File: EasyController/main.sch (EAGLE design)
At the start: 53 parts, among them IC2 L6387EDIP8, IC3 L6387EDIP8, IC4 L6387EDIP8, J3 FUSE, Q1 MOSFET-NCHANNELTO-220-FLAT, Q2 MOSFET-NCHANNELTO-220-FLAT, Q3 MOSFET-NCHANNELTO-220-FLAT, Q4 MOSFET-NCHANNELTO-220-FLAT, Q5 MOSFET-NCHANNELTO-220-FLAT, Q6 MOSFET-NCHANNELTO-220-FLAT

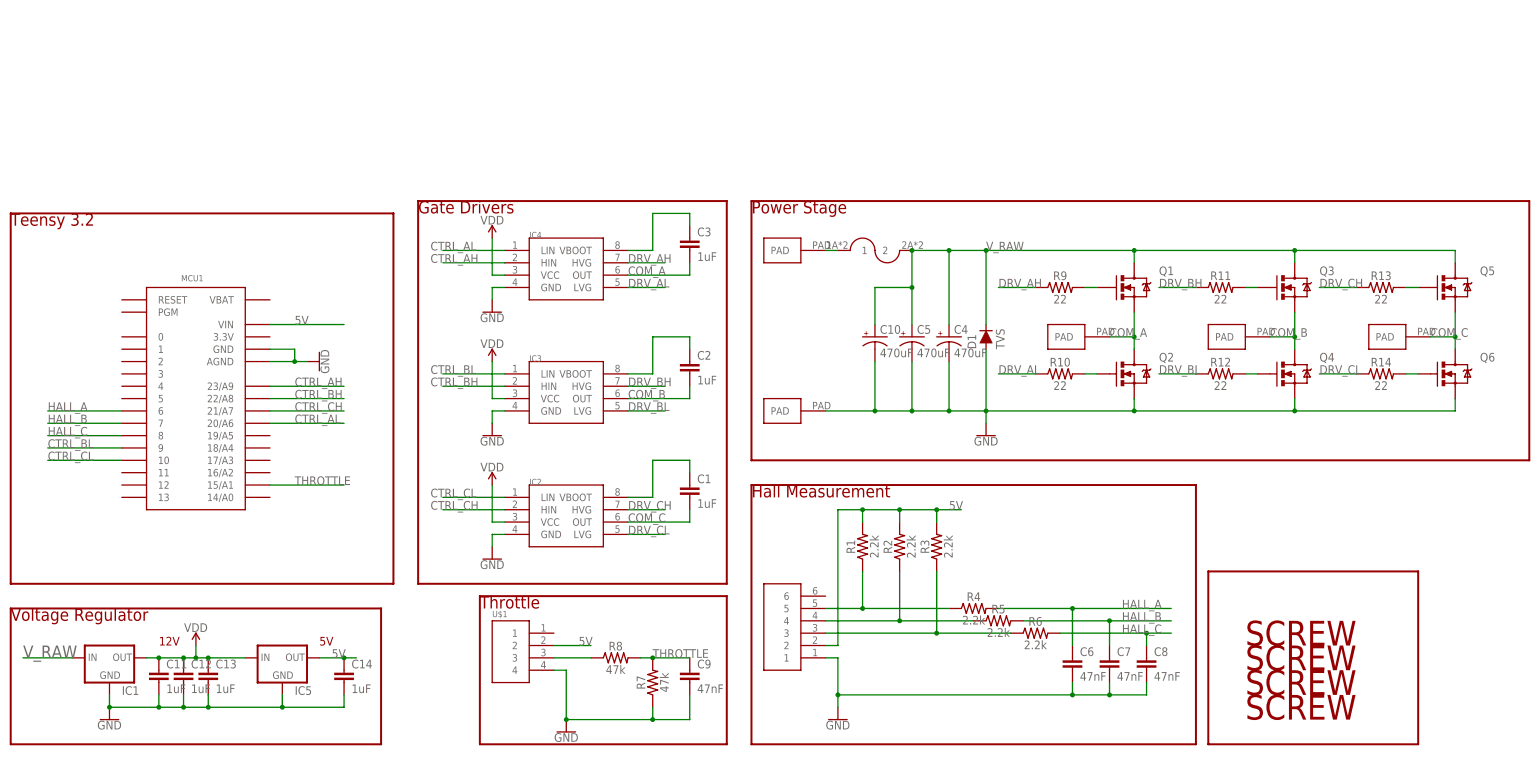
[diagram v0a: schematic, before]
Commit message: CAN transceiver
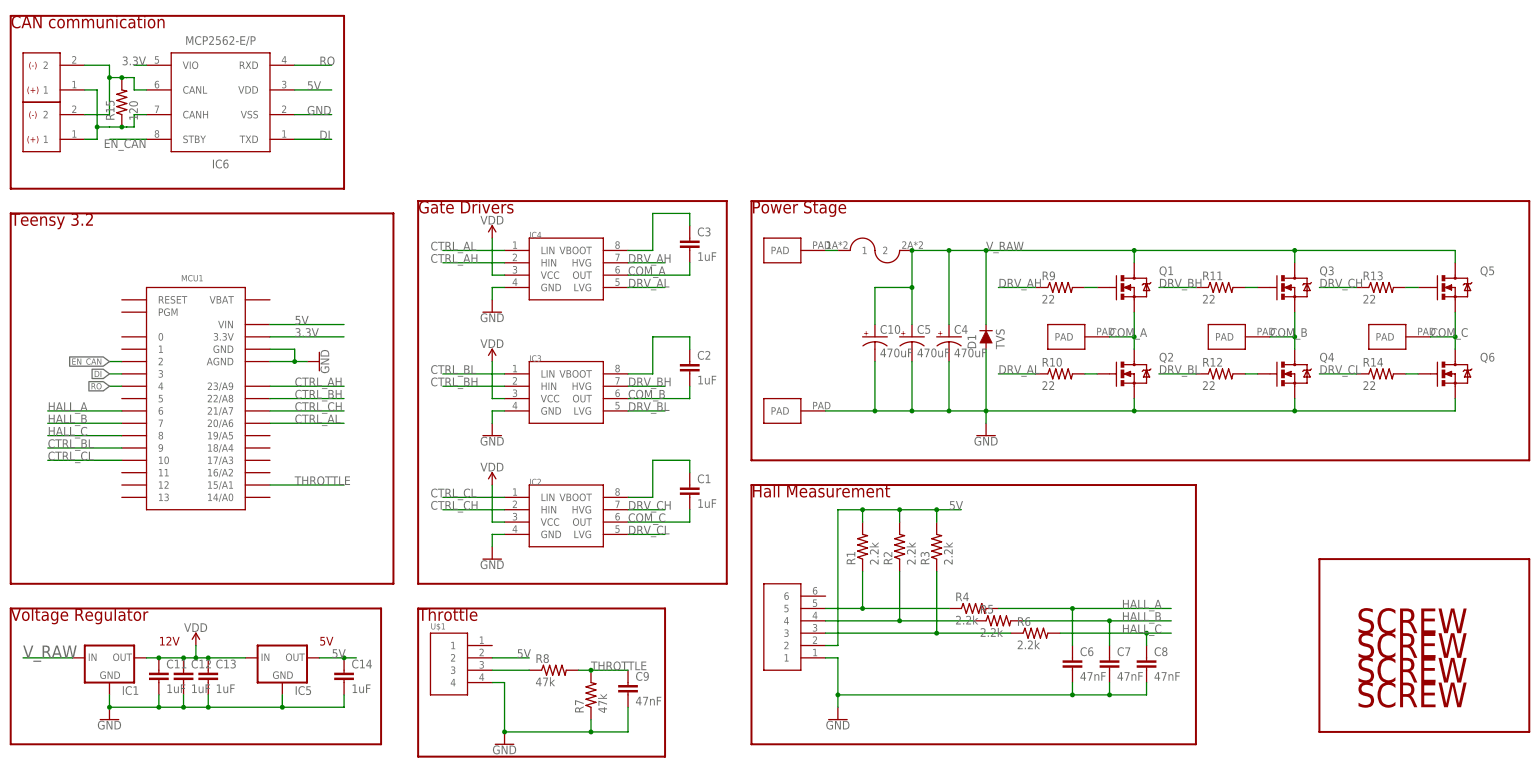
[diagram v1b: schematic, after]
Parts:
- added CAN1, CAN2: HEADER2, Custom_old:HEADER2
- added IC6: MCP2562-E/P, Custom_new:MCP2562-E/P
- added R15: 120, SparkFun-Resistors:RESISTORAXIAL-0.3
- C1, C11, C12, C13, C14, C2, C3, C6, C7, C8, C9: device SparkFun-Capacitors:0.1UF-KIT-EZ-50V-20% -> SparkFun-Capacitors:CAPKIT
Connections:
- new net 3.3V: IC6.VIO, MCU1.3.3V
- new net CANH: CAN1.1, CAN2.1, IC6.CANH, R15.1
- new net CANL: CAN1.2, CAN2.2, IC6.CANL, R15.2
- new net DI: IC6.TXD, MCU1.3
- new net EN_CAN: IC6.STBY, MCU1.2
- new net RO: IC6.RXD, MCU1.4
- net 5V: now also IC6.VDD
- net GND: now also IC6.VSS
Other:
- note added: "CAN communication"
- moved on the sheet: C9, R7, R8, U$1
